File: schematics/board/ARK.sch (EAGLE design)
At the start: 217 parts, among them IC1 STM32F103C8T, Q5 8MHz

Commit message: Разведена плата АРК
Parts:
- removed IC1: STM32F103C8T, micro-stm:STM32F103C8T
- added IC2: STM32F103C8T, CanCubeSat:STM32F103C8T
- R101, R102: value 4k7 -> 5k1
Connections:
- net 1W: now also IC2.PB0; no longer IC1MCU.PB0
- net BMS1: now also IC2.PA5; no longer IC1MCU.PA5
- net BMS2: now also IC2.PA6; no longer IC1MCU.PA6
- net BMS3: now also IC2.PA3; no longer IC1MCU.PA3
- net BMS4: now also IC2.PA4; no longer IC1MCU.PA4
- net BMS5: now also IC2.PA1; no longer IC1MCU.PA1
- net BMS6: now also IC2.PA2; no longer IC1MCU.PA2
- net DPC_RST: now also IC2.PB14; no longer IC1MCU.PB14
- net DPD_RST: now also IC2.PB15; no longer IC1MCU.PB15
- net GND: now also IC2.VSSA; no longer IC1MCU.VSSA
- net I2CINT: now also IC2.PB7; no longer IC1MCU.PB7
- net N$133: now also IC2.OSC_OUT; no longer IC1MCU.OSC_OUT
- net N$145: now also IC2.OSC_IN; no longer IC1MCU.OSC_IN
- net N$148: now also IC2.PC15; no longer IC1MCU.PC15
- net N$152: now also IC2.PC14; no longer IC1MCU.PC14
- net N$156: now also IC2.PA15; no longer IC1MCU.PA15
- net N$157: now also IC2.PB3; no longer IC1MCU.PB3
- net N$161: now also IC2.PB5; no longer IC1MCU.PB5
- net NRST: now also IC2.NRST; no longer IC1MCU.NRST
- net PGOOD1: now also IC2.PB1; no longer IC1MCU.PB1
- net PGOOD2: now also IC2.PB2; no longer IC1MCU.PB2
- net RX-C: now also IC2.PA10; no longer IC1MCU.PA10
- net SCL: now also IC2.PB10; no longer IC1MCU.PB10
- net SCLTM: now also IC2.PB8; no longer IC1MCU.PB8
- net SDA: now also IC2.PB11; no longer IC1MCU.PB11
- net SDATM: now also IC2.PB9; no longer IC1MCU.PB9
- net SWC: now also IC2.PA14; no longer IC1MCU.PA14
- net SWD: now also IC2.PA13; no longer IC1MCU.PA13
- net TIME: now also IC2.PB6; no longer IC1MCU.PB6
- net TX-C: now also IC2.PA9; no longer IC1MCU.PA9
- net VDD: now also IC2.VDDA; no longer IC1MCU.VDDA

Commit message: Разведена плата БСК1
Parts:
- renumbered LED1 to PWR, LED2 to PB5, VAR4 to BSK4, VAR5A to AB1, VAR5B to AB2, VAR5C to AB3

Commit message: С АРКом всё плохо. Надо снова переделывать(
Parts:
- removed C15, C16: 0,1µ, rcl:C-USC0603
- removed R31, R58: R01, rcl:R-US_R2512
- removed R32, R57, R59, R60: 10R, resistor:R-US_R0603
- removed U$2, U$9: INA219AID, CanCubeSat:INA219AID
- R30: value 150k -> 14K3
- R61: value 680k -> 91K
- R70: value 150k -> 14k3
- R72: value 680k -> 91k
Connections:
- removed net N$134: C35.1, R72.2, R75.1, R77.1, U$59.PVOUT
- removed net N$137: C37.1, R65.2, R71.1, R74.1, R87.2, U$59.PVIN, U$59.VIN
- removed net N$14: C50.1, R31.1, R57.1, R63.2, U$16.PVIN, U$16.VIN
- removed net N$140: C39.1, U$59.SVCC, U$59.VCC
- removed net N$143: R70.2, R72.1, U$59.FB
- removed net N$31: R30.2, R61.1, U$16.FB
- removed net N$49: C16.2, R60.2, U$2.IN-
- removed net N$50: C49.1, R58.1, R60.1, R61.2, U$16.PVOUT
- new net INA_BMS+: C35.1, C50.1, R63.2, R72.2, R75.1, R77.1, U$16.PVIN, U$16.VIN, U$59.PVOUT
- new net INA_BUS+: C37.1, C49.1, R61.2, R65.2, R71.1, R74.1, R87.2, U$16.PVOUT, U$59.PVIN, U$59.VIN
- net BMS+: no longer R31.2, R32.1
- net BUS+: no longer R58.2, R59.1
- net GND: now also R30.2, R70.1; no longer AD5272#2.VSS, AD5272#2.W, C29.2, U$2.A1, U$2.GND, U$60.GND, U$9.A0, U$9.A1, U$9.GND
- net N$25: now also R72.1, U$59.FB; no longer C32.1, C43.1, R70.1, U$60.VDD
- net N$26: now also R70.2, U$60.GND; no longer C31.1, U$16.MPPC, U$16.SVCC, U$16.VCC
- net N$45: now also C32.1, C39.1, C43.1, U$59.SVCC, U$59.VCC, U$60.VDD; no longer C15.1, R32.2, U$9.IN+
- net N$47: now also AD5272#2.VDD, C31.1, C51.1, C52.1, U$16.MPPC, U$16.SVCC, U$16.VCC; no longer C15.2, R57.2, U$9.IN-
- net N$48: now also AD5272#2.VSS, AD5272#2.W, C29.2, R30.1; no longer C16.1, R59.2, U$2.IN+
- net N$5: now also R61.1, U$16.FB; no longer AD5272#2.VDD, C51.1, C52.1, R30.1
- net SCL: no longer U$2.SCL, U$9.SCL
- net SDA: no longer U$2.SDA, U$9.SDA
- net VDD: no longer U$2.A0, U$2.VCC, U$9.VCC
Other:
- moved on the sheet: R30, R70

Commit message: Изменения в компоновке БКУ
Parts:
- removed R25, R26: 10k, resistor:R-US_R0603
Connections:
- removed net N$156: IC2.PA15, R25.2
- removed net N$157: IC2.PB3, R26.2
- net VDD: no longer R25.1, R26.1
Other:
- moved on the sheet: R27, R64
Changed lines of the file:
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@@
 <part name="PWR" library="led" library_urn="urn:adsk.eagle:library:259" deviceset="LED" device="CHIPLED_0603" package3d_urn="urn:adsk.eagle:package:15822/2"/>
 <part name="PB5" library="led" library_urn="urn:adsk.eagle:library:259" deviceset="LED" device="CHIPLED_0603" package3d_urn="urn:adsk.eagle:package:15822/2"/>
-<part name="R25" library="resistor" library_urn="urn:adsk.eagle:library:348" deviceset="R-US_" device="R0603" package3d_urn="urn:adsk.eagle:package:23555/3" value="10k"/>
-<part name="R26" library="resistor" library_urn="urn:adsk.eagle:library:348" deviceset="R-US_" device="R0603" package3d_urn="urn:adsk.eagle:package:23555/3" value="10k"/>
 <part name="R27" library="resistor" library_urn="urn:adsk.eagle:library:348" deviceset="R-US_" device="R0603" package3d_urn="urn:adsk.eagle:package:23555/3" value="10k"/>
 <part name="R64" library="resistor" library_urn="urn:adsk.eagle:library:348" deviceset="R-US_" device="R0603" package3d_urn="urn:adsk.eagle:package:23555/3" value="10k"/>
@@
 <attribute name="VALUE" x="536.448" y="276.225" size="1.778" layer="96"/>
 </instance>
-<instance part="R25" gate="G$1" x="490.22" y="281.94" smashed="yes">
+<instance part="R27" gate="G$1" x="490.22" y="289.56" smashed="yes">
+<attribute name="NAME" x="486.41" y="291.0586" size="1.778" layer="95"/>
+<attribute name="VALUE" x="486.41" y="286.258" size="1.778" layer="96"/>
+</instance>
+<instance part="R64" gate="G$1" x="490.22" y="281.94" smashed="yes">
 <attribute name="NAME" x="486.41" y="283.4386" size="1.778" layer="95"/>
 <attribute name="VALUE" x="486.41" y="278.638" size="1.778" layer="96"/>
 </instance>
-<instance part="R26" gate="G$1" x="490.22" y="274.32" smashed="yes">
-<attribute name="NAME" x="486.41" y="275.8186" size="1.778" layer="95"/>
-<attribute name="VALUE" x="486.41" y="271.018" size="1.778" layer="96"/>
-</instance>
-<instance part="R27" gate="G$1" x="490.22" y="266.7" smashed="yes">
-<attribute name="NAME" x="486.41" y="268.1986" size="1.778" layer="95"/>
-<attribute name="VALUE" x="486.41" y="263.398" size="1.778" layer="96"/>
-</instance>
-<instance part="R64" gate="G$1" x="490.22" y="259.08" smashed="yes">
-<attribute name="NAME" x="486.41" y="260.5786" size="1.778" layer="95"/>
-<attribute name="VALUE" x="486.41" y="255.778" size="1.778" layer="96"/>
-</instance>
 <instance part="R81" gate="G$1" x="530.86" y="281.94" smashed="yes">
 <attribute name="NAME" x="527.05" y="283.4386" size="1.778" layer="95"/>
@@
 </segment>
 <segment>
-<wire x1="482.6" y1="281.94" x2="482.6" y2="274.32" width="0.1524" layer="91"/>
-<label x="482.6" y="246.38" size="1.778" layer="95" rot="R90"/>
-<pinref part="R25" gate="G$1" pin="1"/>
-<wire x1="482.6" y1="274.32" x2="482.6" y2="266.7" width="0.1524" layer="91"/>
-<wire x1="482.6" y1="266.7" x2="482.6" y2="259.08" width="0.1524" layer="91"/>
-<wire x1="485.14" y1="281.94" x2="482.6" y2="281.94" width="0.1524" layer="91"/>
-<pinref part="R26" gate="G$1" pin="1"/>
-<wire x1="485.14" y1="274.32" x2="482.6" y2="274.32" width="0.1524" layer="91"/>
-<junction x="482.6" y="274.32"/>
+<label x="482.6" y="269.24" size="1.778" layer="95" rot="R90"/>
+<wire x1="482.6" y1="289.56" x2="482.6" y2="281.94" width="0.1524" layer="91"/>
 <pinref part="R27" gate="G$1" pin="1"/>
-<wire x1="485.14" y1="266.7" x2="482.6" y2="266.7" width="0.1524" layer="91"/>
-<junction x="482.6" y="266.7"/>
+<wire x1="485.14" y1="289.56" x2="482.6" y2="289.56" width="0.1524" layer="91"/>
 <pinref part="R64" gate="G$1" pin="1"/>
-<wire x1="485.14" y1="259.08" x2="482.6" y2="259.08" width="0.1524" layer="91"/>
-<wire x1="482.6" y1="259.08" x2="482.6" y2="246.38" width="0.1524" layer="91"/>
-<junction x="482.6" y="259.08"/>
+<wire x1="485.14" y1="281.94" x2="482.6" y2="281.94" width="0.1524" layer="91"/>
+<wire x1="482.6" y1="281.94" x2="482.6" y2="269.24" width="0.1524" layer="91"/>
+<junction x="482.6" y="281.94"/>
 </segment>
 <segment>
@@
 </segment>
 </net>
-<net name="N$156" class="0">
-<segment>
-<wire x1="505.46" y1="281.94" x2="505.46" y2="302.26" width="0.1524" layer="91"/>
-<wire x1="505.46" y1="302.26" x2="502.92" y2="302.26" width="0.1524" layer="91"/>
-<wire x1="505.46" y1="281.94" x2="495.3" y2="281.94" width="0.1524" layer="91"/>
-<wire x1="502.92" y1="302.26" x2="502.92" y2="312.42" width="0.1524" layer="91"/>
-<pinref part="R25" gate="G$1" pin="2"/>
-<pinref part="IC2" gate="MCU" pin="PA15"/>
-</segment>
-</net>
-<net name="N$157" class="0">
-<segment>
-<wire x1="502.92" y1="274.32" x2="502.92" y2="299.72" width="0.1524" layer="91"/>
-<wire x1="502.92" y1="299.72" x2="515.62" y2="299.72" width="0.1524" layer="91"/>
-<wire x1="502.92" y1="274.32" x2="495.3" y2="274.32" width="0.1524" layer="91"/>
-<wire x1="515.62" y1="299.72" x2="515.62" y2="312.42" width="0.1524" layer="91"/>
-<pinref part="R26" gate="G$1" pin="2"/>
-<pinref part="IC2" gate="MCU" pin="PB3"/>
-</segment>
-</net>
 <net name="N$159" class="0">
 <segment>
@@
 <net name="SWC" class="0">
 <segment>
-<wire x1="500.38" y1="266.7" x2="500.38" y2="312.42" width="0.1524" layer="91"/>
-<wire x1="500.38" y1="266.7" x2="495.3" y2="266.7" width="0.1524" layer="91"/>
+<wire x1="500.38" y1="289.56" x2="500.38" y2="312.42" width="0.1524" layer="91"/>
+<wire x1="500.38" y1="289.56" x2="495.3" y2="289.56" width="0.1524" layer="91"/>
 <pinref part="R27" gate="G$1" pin="2"/>
 <label x="500.38" y="302.26" size="1.778" layer="95" rot="R90"/>
@@
 <net name="SWD" class="0">
 <segment>
-<wire x1="497.84" y1="259.08" x2="497.84" y2="312.42" width="0.1524" layer="91"/>
-<wire x1="497.84" y1="259.08" x2="495.3" y2="259.08" width="0.1524" layer="91"/>
+<wire x1="497.84" y1="281.94" x2="497.84" y2="312.42" width="0.1524" layer="91"/>
+<wire x1="497.84" y1="281.94" x2="495.3" y2="281.94" width="0.1524" layer="91"/>
 <pinref part="R64" gate="G$1" pin="2"/>
 <label x="497.84" y="302.26" size="1.778" layer="95" rot="R90"/>

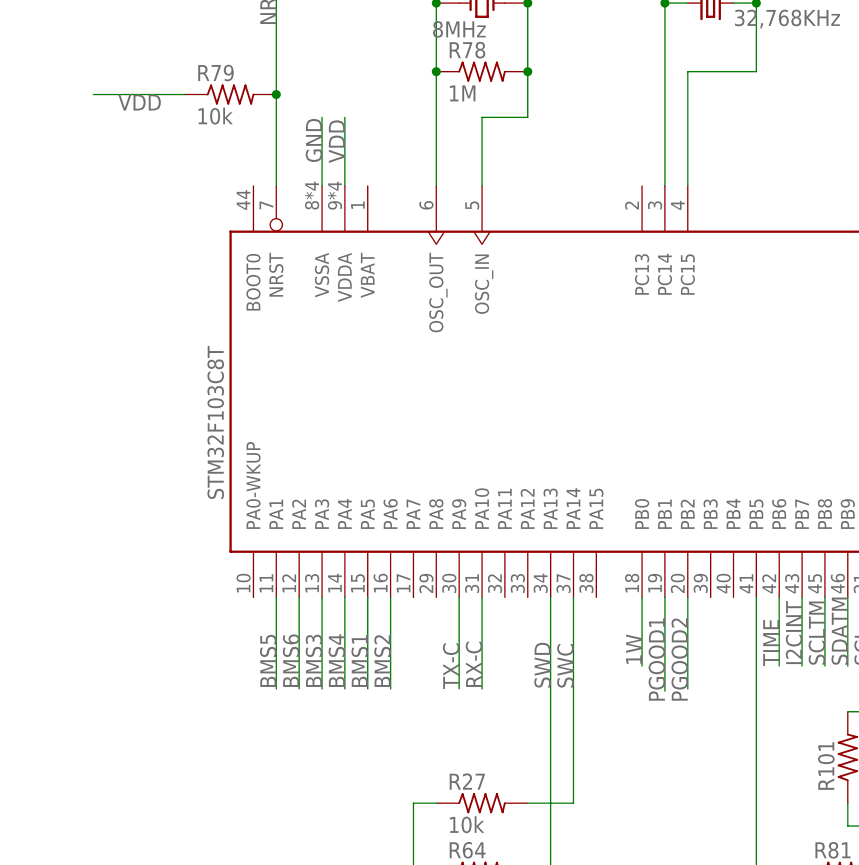
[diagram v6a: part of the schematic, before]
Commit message: Исправлены АРК и БСК1
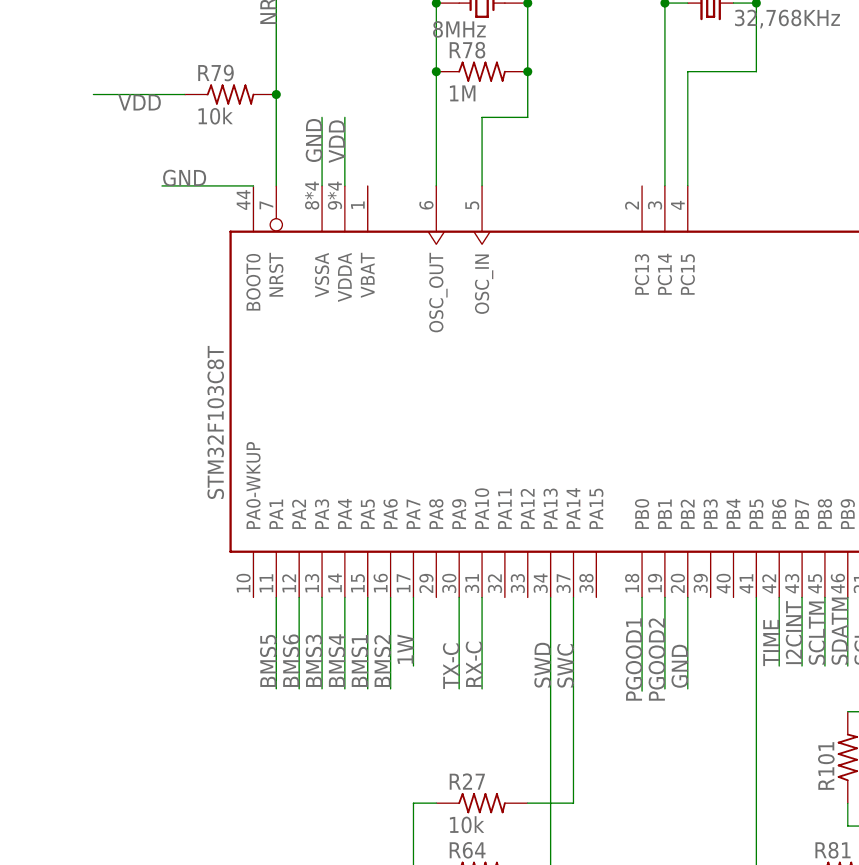
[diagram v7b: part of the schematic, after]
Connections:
- net 1W: now also IC2.PA7; no longer IC2.PB0
- net GND: now also IC2.BOOT0, IC2.PB2
- net PGOOD1: now also IC2.PB0; no longer IC2.PB1
- net PGOOD2: now also IC2.PB1; no longer IC2.PB2
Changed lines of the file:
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@@
 <?xml version="1.0" encoding="utf-8"?>
 <!DOCTYPE eagle SYSTEM "eagle.dtd">
-<eagle version="9.6.0">
+<eagle version="9.4.2">
 <drawing>
 <settings>
@@
 <label x="680.72" y="101.6" size="1.778" layer="95" rot="R90"/>
 </segment>
+<segment>
+<pinref part="IC2" gate="MCU" pin="BOOT0"/>
+<wire x1="464.82" y1="358.14" x2="454.66" y2="358.14" width="0.1524" layer="91"/>
+<label x="454.66" y="358.14" size="1.778" layer="95"/>
+</segment>
+<segment>
+<pinref part="IC2" gate="MCU" pin="PB2"/>
+<wire x1="513.08" y1="312.42" x2="513.08" y2="302.26" width="0.1524" layer="91"/>
+<label x="513.08" y="302.26" size="1.778" layer="95" rot="R90"/>
+</segment>
 </net>
 <net name="INA_BUS+" class="0">
@@
 <net name="1W" class="0">
 <segment>
-<wire x1="508" y1="312.42" x2="508" y2="304.8" width="0.1524" layer="91"/>
-<label x="508" y="304.8" size="1.778" layer="95" rot="R90"/>
-<pinref part="IC2" gate="MCU" pin="PB0"/>
-</segment>
-<segment>
 <pinref part="AB1" gate="A" pin="5"/>
 <wire x1="205.74" y1="25.4" x2="205.74" y2="43.18" width="0.1524" layer="91"/>
@@
 <label x="198.12" y="289.56" size="1.778" layer="95" rot="R90"/>
 </segment>
+<segment>
+<wire x1="482.6" y1="312.42" x2="482.6" y2="304.8" width="0.1524" layer="91"/>
+<label x="482.6" y="304.8" size="1.778" layer="95" rot="R90"/>
+<pinref part="IC2" gate="MCU" pin="PA7"/>
+</segment>
 </net>
 <net name="N$147" class="0">
@@
 </segment>
 <segment>
-<wire x1="513.08" y1="312.42" x2="513.08" y2="302.26" width="0.1524" layer="91"/>
-<label x="513.08" y="300.736" size="1.778" layer="95" rot="R90"/>
-<pinref part="IC2" gate="MCU" pin="PB2"/>
+<wire x1="510.54" y1="312.42" x2="510.54" y2="302.26" width="0.1524" layer="91"/>
+<label x="510.54" y="300.736" size="1.778" layer="95" rot="R90"/>
+<pinref part="IC2" gate="MCU" pin="PB1"/>
 </segment>
 </net>
@@
 <net name="PGOOD1" class="0">
 <segment>
-<wire x1="510.54" y1="312.42" x2="510.54" y2="302.006" width="0.1524" layer="91"/>
-<label x="510.54" y="300.736" size="1.778" layer="95" rot="R90"/>
-<pinref part="IC2" gate="MCU" pin="PB1"/>
-</segment>
-<segment>
 <pinref part="U$59" gate="G$1" pin="PGOOD"/>
 <wire x1="485.14" y1="135.89" x2="474.218" y2="135.89" width="0.1524" layer="91"/>
 <label x="473.202" y="136.144" size="1.778" layer="95"/>
 </segment>
+<segment>
+<wire x1="508" y1="312.42" x2="508" y2="302.006" width="0.1524" layer="91"/>
+<label x="508" y="300.736" size="1.778" layer="95" rot="R90"/>
+<pinref part="IC2" gate="MCU" pin="PB0"/>
+</segment>
 </net>
